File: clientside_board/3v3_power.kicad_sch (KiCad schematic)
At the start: 29 parts, among them U3 INA180A3, U4 TPS62160DGK, U5 INA180A3, U6 INA180A3, U7 INA180A3

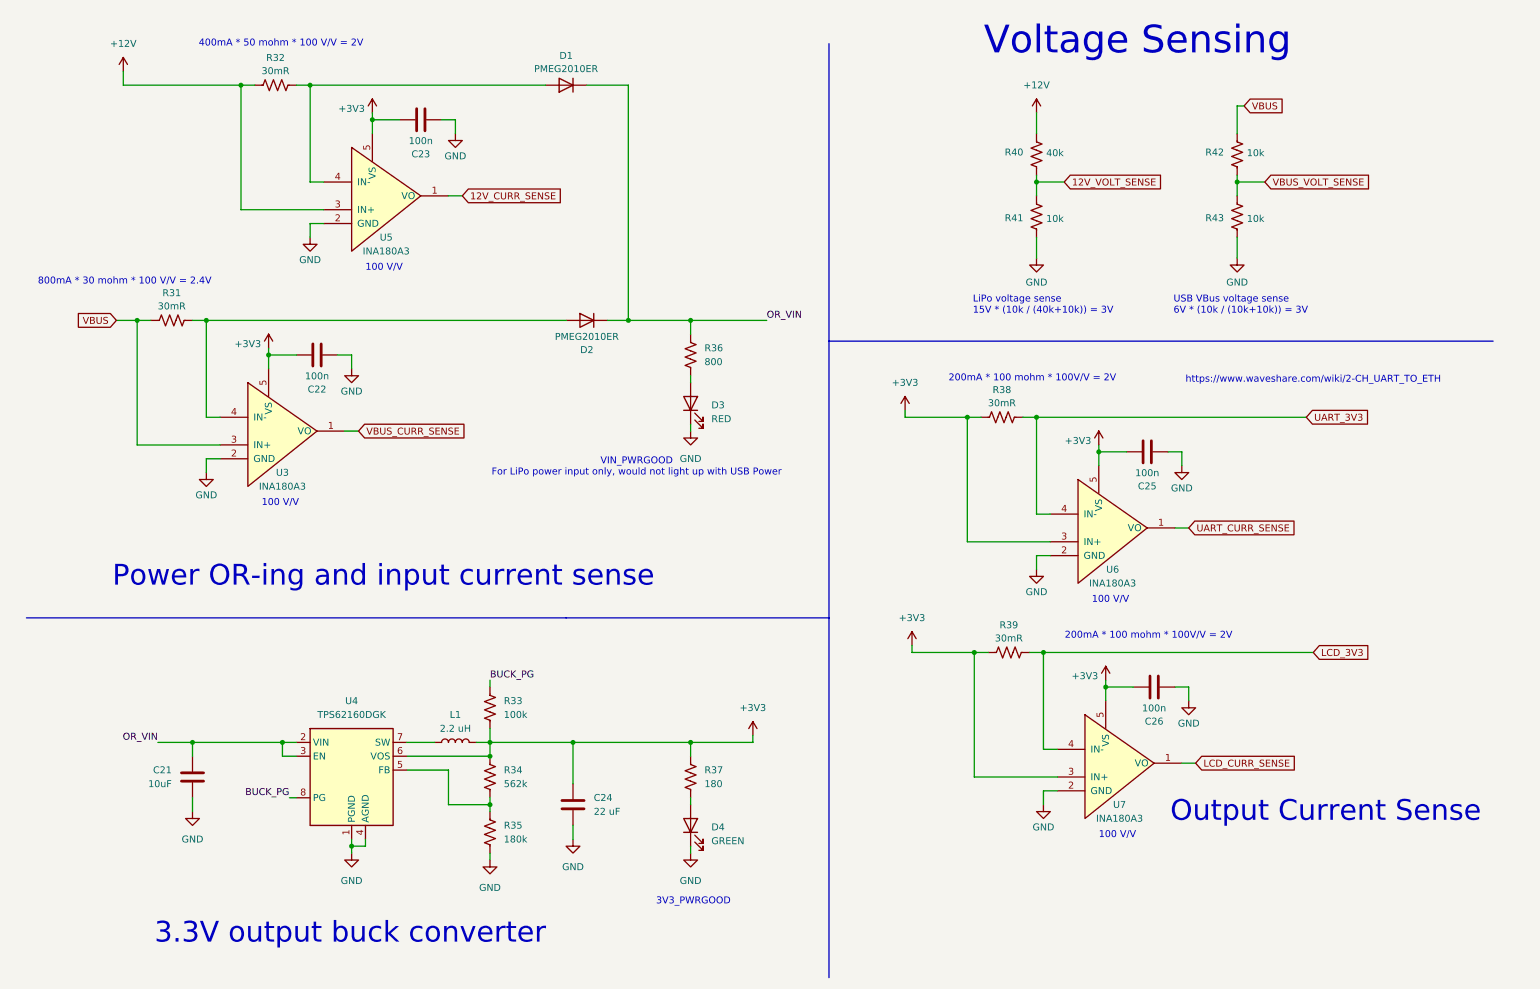
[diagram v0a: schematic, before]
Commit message: Update power for 5V LCD display
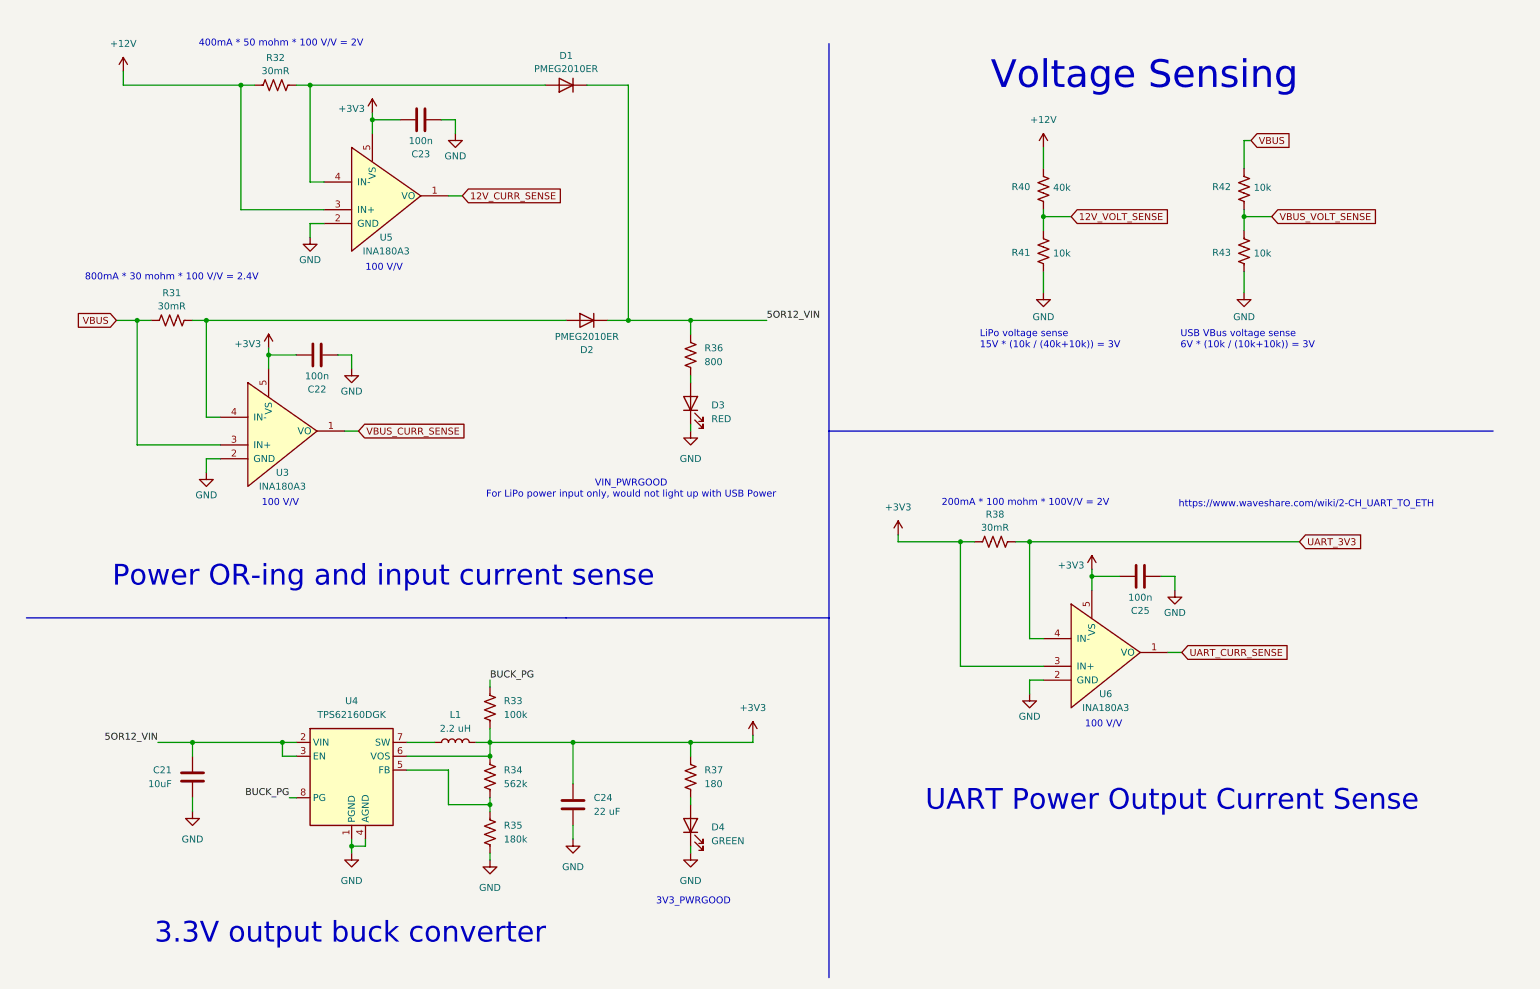
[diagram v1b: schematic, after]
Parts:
- removed C26: 100n, Capacitor_SMD:C_0805_2012Metric_Pad1.18x1.45mm_HandSolder, symbol Device:C
- removed R39: 30mR, Resistor_SMD:R_0805_2012Metric_Pad1.20x1.40mm_HandSolder, symbol Device:R_US
- removed U7: INA180A3, Package_TO_SOT_SMD:SOT-23-5_HandSoldering, symbol canhw:INA180
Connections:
- net OR_VIN renamed 5OR12_VIN
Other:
- note added: "UART Power Output Current Sense"
- note removed: "Output Current Sense"
- moved on the sheet: C25, R38, R40, R41, R42, R43, U6

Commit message: Top sheet update
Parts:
- C28: renamed from C21; footprint Capacitor_SMD:C_0805_2012Metric_Pad1.18x1.45mm_HandSolder -> Capacitor_SMD:C_0603_1608Metric_Pad1.08x0.95mm_HandSolder
- C29: renamed from C22; footprint Capacitor_SMD:C_0805_2012Metric_Pad1.18x1.45mm_HandSolder -> Capacitor_SMD:C_0603_1608Metric_Pad1.08x0.95mm_HandSolder
- C30: renamed from C23; footprint Capacitor_SMD:C_0805_2012Metric_Pad1.18x1.45mm_HandSolder -> Capacitor_SMD:C_0603_1608Metric_Pad1.08x0.95mm_HandSolder
- C31: renamed from C24; footprint Capacitor_SMD:C_0805_2012Metric_Pad1.18x1.45mm_HandSolder -> Capacitor_SMD:C_0603_1608Metric_Pad1.08x0.95mm_HandSolder
- C32: renamed from C25; footprint Capacitor_SMD:C_0805_2012Metric_Pad1.18x1.45mm_HandSolder -> Capacitor_SMD:C_0603_1608Metric_Pad1.08x0.95mm_HandSolder
- renumbered R31 to R38, R32 to R39, R33 to R40, R34 to R41, R35 to R42, R36 to R43, R37 to R44, R38 to R45, R40 to R46, R41 to R47, R42 to R48, R43 to R49, U3 to U6, U4 to U7, U5 to U8, U6 to U9
